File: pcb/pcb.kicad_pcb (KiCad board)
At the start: 4 copper layers, 40 x 15 mm, 20 parts, among them J1 Conn_01x04_MountingPin, J2 Conn_01x04_MountingPin, J4 Conn_ARM_SWD_TagConnect_TC203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, U1 MCP2542FDxMF, U2 STM32G0B1KBUx, U3 MCP1792x-3302xCB

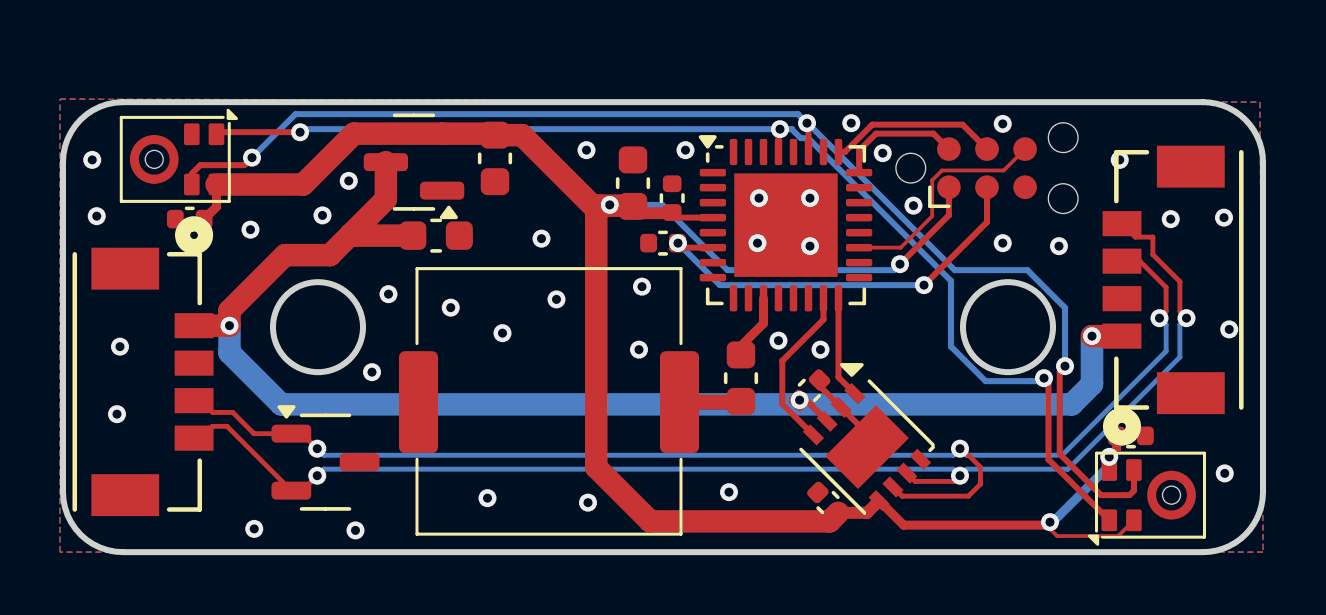
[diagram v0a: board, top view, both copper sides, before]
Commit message: add source termination
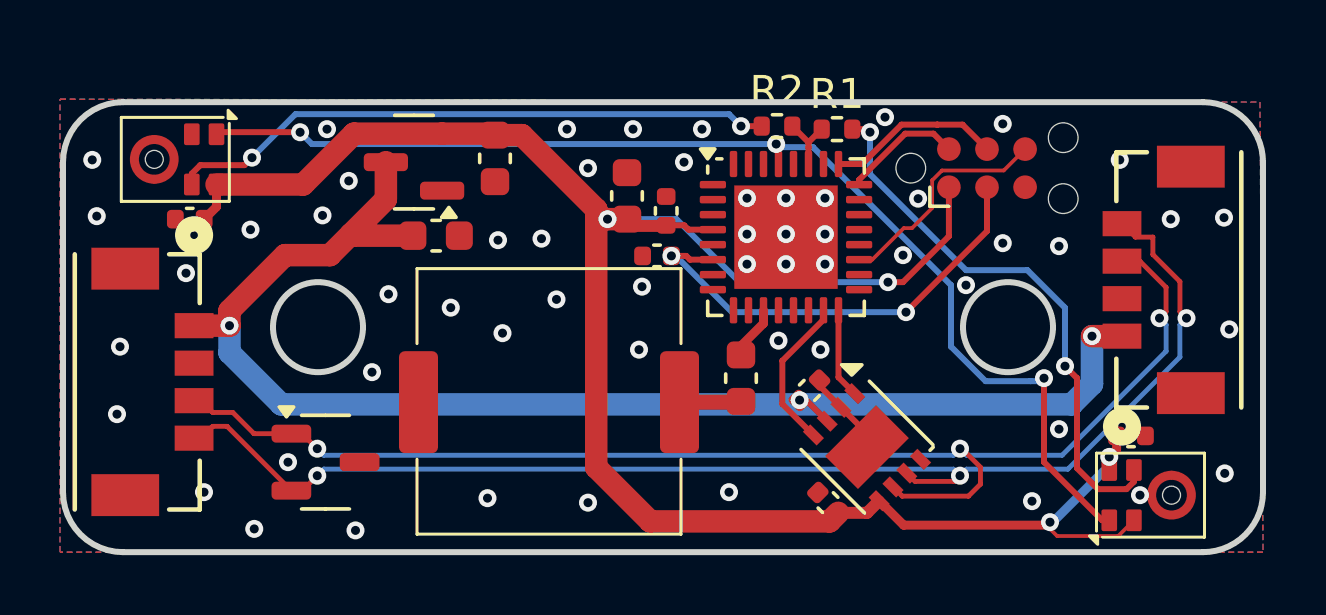
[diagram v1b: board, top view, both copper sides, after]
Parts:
- added R1: R_Small, Resistor_SMD:R_0402_1005Metric, F.Cu at (204.5, 52.5)
- added R2: R_Small, Resistor_SMD:R_0402_1005Metric, F.Cu at (202.5, 52.4)
- moved C11 0.47 mm to (198.5, 56.7)
- moved C12 0.47 mm to (198.8, 55.2)
- moved C13 0.47 mm to (197.5, 54.7)
- moved U2 0.40 mm to (202.8, 56.1)
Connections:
- M3 pad 4: /I2S_CLK -> Net-(M3-CLK)
- M4 pad 4: /I2S_CLK -> Net-(M4-CLK)
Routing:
- net /I2S_CLK: track 42.7 -> 2.11 mm, vias 3 -> 0
- net Net-(M3-CLK): track 0.00 -> 20.3 mm, vias 0 -> 2
- net Net-(M4-CLK): track 0.00 -> 18.6 mm, vias 0 -> 2
- net /RESET: track 14.2 -> 15.3 mm
- net +3V3: track 66.1 -> 67.0 mm
- net GND: vias 39 -> 56

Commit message: fix drc
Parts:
- moved C13 0.55 mm to (197.9, 54.4)
- moved C12 0.51 mm to (199.2, 54.9)
- moved C11 0.33 mm to (198.5, 56.4)
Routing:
- net GND: vias 56 -> 53

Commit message: add rs485
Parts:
- removed C10, C9: 100n, Capacitor_SMD:C_0402_1005Metric
- C1, C2: value 2.2u -> 10u
- C12, C15, C16: value 100n -> 10u
- C13: value 4.7u -> 10u
- D1: value CAN_TVS -> TVS
- LS1: moved to B.Cu
- U1: value MCP2542FDxMF -> THVD1451; footprint Package_DFN_QFN:DFN-8-1EP_3x3mm_P0.65mm_EP1.55x2.4mm -> Package_SON:VSON-10-1EP_3x3mm_P0.5mm_EP1.65x2.4mm
- U3: value MCP1792x-3302xCB -> AP2210; footprint Package_TO_SOT_SMD:SOT-23 -> Package_TO_SOT_SMD:SOT-23-3
- moved LS1 4.52 mm to (198.6, 59.0), turned to -90 degrees
- moved C14 1.35 mm to (200.0, 60.5), turned to 180 degrees
- moved U1 1.00 mm to (206.5, 63.1)
- moved R1 0.12 mm to (204.6, 52.4), turned to 180 degrees
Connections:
- net /CAN_RX renamed /TX
- net /CAN_TX renamed /RX
- net Net-(M3-CLK) renamed /CLK_1
- D1 pad 1: /CAN- -> /RS485-
- D1 pad 2: /CAN+ -> /RS485+
- J1 pad 3: /CAN- -> /RS485-
- J1 pad 4: /CAN+ -> /RS485+
- J2 pad 3: /CAN- -> /RS485-
- J2 pad 4: /CAN+ -> /RS485+
- M4 pad 4: Net-(M4-CLK) -> /CLK_2
- R1 pad 1: /I2S_CLK -> /CLK_2
- R1 pad 2: Net-(M4-CLK) -> Net-(U2-PB3)
- R2 pad 2: /I2S_CLK -> Net-(U2-PB3)
- U1 pad 2: GND -> /RX_EN
- U1 pad 3: +5V -> /TX_EN
- U1 pad 5: +3V3 -> /TERM
- U1 pad 6: /CAN- -> GND
- U1 pad 7: /CAN+ -> /SLR
- U1 pad 8: /STBY -> /RS485+
- U1 pad 9: GND -> /RS485-
- U2 pad 12: unconnected-(U2-PA5-Pad12) -> /SLR
- U2 pad 13: unconnected-(U2-PA6-Pad13) -> /TERM
- U2 pad 14: unconnected-(U2-PA7-Pad14) -> /TX_EN
- U2 pad 17: unconnected-(U2-PB2-Pad17) -> /RX_EN
- U2 pad 27: /I2S_CLK -> Net-(U2-PB3)
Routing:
- net /RS485+: track 0.00 -> 44.8 mm, vias 0 -> 3
- net /CAN+: track 43.7 -> 0.00 mm, vias 3 -> 0
- net /CAN-: track 43.6 -> 0.00 mm, vias 3 -> 0
- net /RS485-: track 0.00 -> 42.4 mm, vias 0 -> 3
- net /CLK_2: track 0.00 -> 18.8 mm, vias 0 -> 2
- net Net-(M4-CLK): track 18.6 -> 0.00 mm, vias 2 -> 0
- net +3V3: track 66.7 -> 54.5 mm
- net /SLR: track 0.00 -> 11.5 mm
- net Net-(C14-Pad2): track 2.08 -> 7.50 mm, vias 0 -> 1
- net /RX_EN: track 0.00 -> 5.40 mm, vias 0 -> 2
- net /TERM: track 0.00 -> 5.07 mm
- net /TX_EN: track 0.00 -> 4.39 mm, vias 0 -> 2
- net Net-(U2-PB3): track 0.00 -> 2.11 mm
- net /I2S_CLK: track 2.11 -> 0.00 mm
- net /RESET: track 14.8 -> 16.7 mm
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
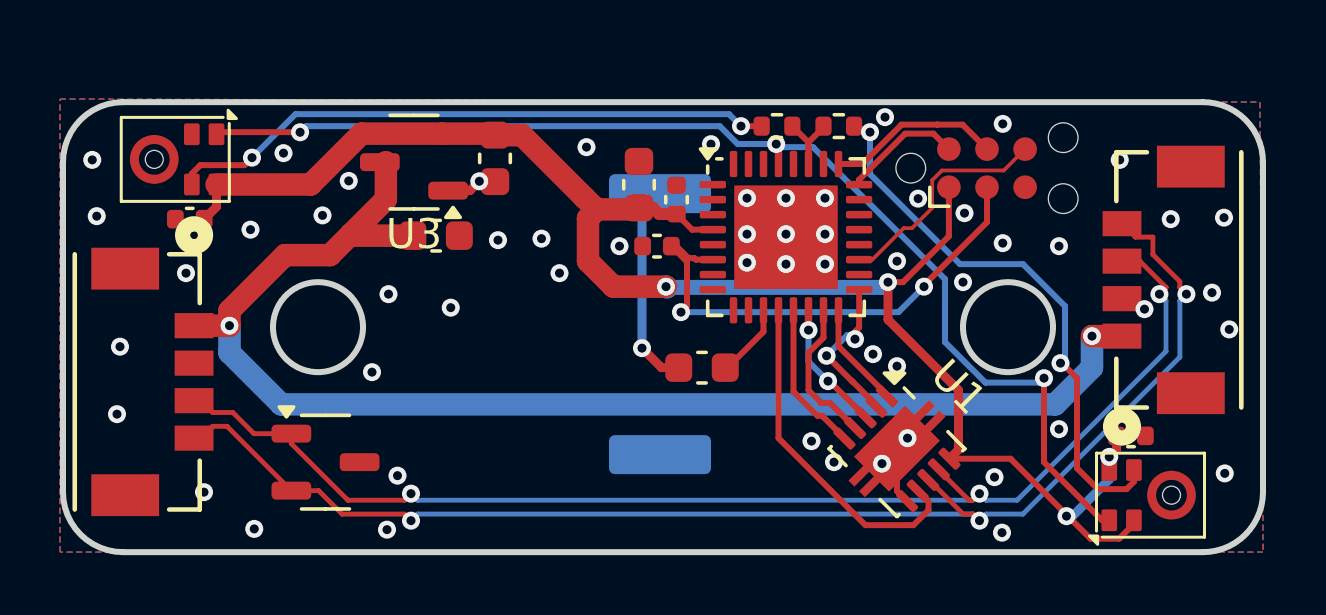
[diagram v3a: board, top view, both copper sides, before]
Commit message: rs485 re route
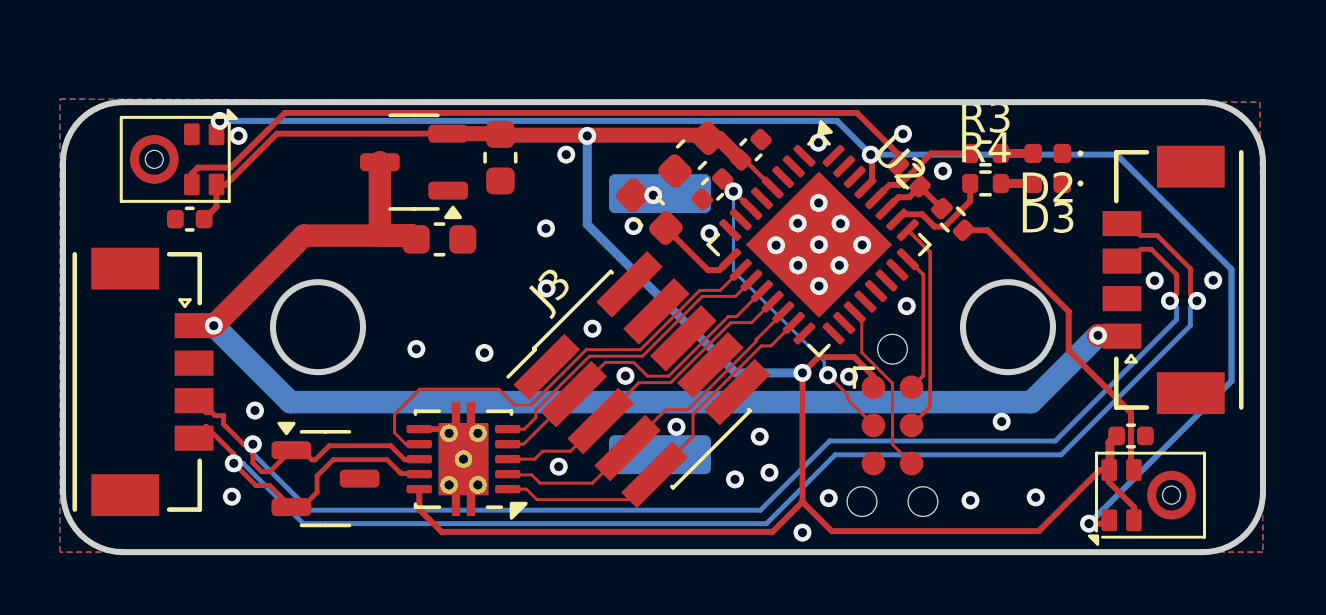
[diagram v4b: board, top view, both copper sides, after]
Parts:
- added D2: LED, Diode_SMD:D_0402_1005Metric, F.Cu at (211.5, 53.3)
- added D3: LED, Diode_SMD:D_0402_1005Metric, F.Cu at (211.5, 54.3)
- added J3: DEBUG, Connector_PinHeader_1.27mm:PinHeader_2x05_P1.27mm_Vertical_SMD, F.Cu at (198.0, 60.9)
- added R3: R_Small, Resistor_SMD:R_0402_1005Metric, F.Cu at (209.4, 53.3)
- added R4: R_Small, Resistor_SMD:R_0402_1005Metric, F.Cu at (209.4, 54.3)
- U1: footprint Package_SON:VSON-10-1EP_3x3mm_P0.5mm_EP1.65x2.4mm -> Package_SON:VSON-10-1EP_3x3mm_P0.5mm_EP1.65x2.4mm_ThermalVias
- moved U1 14.5 mm to (192.1, 63.5), turned to 180 degrees
- moved J4 9.14 mm to (206.3, 62.4), turned to -90 degrees
- moved C14 5.49 mm to (198.2, 55.2), turned to 135 degrees
- moved R1 4.91 mm to (208.4, 55.5), turned to 135 degrees
- moved R2 4.70 mm to (206.9, 54.1), turned to -45 degrees
- moved C12 2.99 mm to (201.6, 53.2), turned to 45 degrees
- moved C11 2.65 mm to (200.3, 54.5), turned to 45 degrees
- moved C13 2.02 mm to (199.7, 53.4), turned to -135 degrees
- moved U2 1.13 mm to (203.9, 56.4), turned to -45 degrees
- moved D1 0.55 mm to (187.4, 64.2)
- moved C1 0.18 mm to (193.3, 53.5)
- moved C2 0.17 mm to (191.2, 56.2)
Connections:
- D1 pad 1: /RS485- -> /RS485+
- D1 pad 2: /RS485+ -> /RS485-
- J1 pad 3: /RS485- -> /RS485+
- J1 pad 4: /RS485+ -> /RS485-
- J2 pad 3: /RS485- -> /RS485+
- J2 pad 4: /RS485+ -> /RS485-
- U2 pad 10: unconnected-(U2-PA3-Pad10) -> /SLR
- U2 pad 11: /SPEAKER -> /TERM
- U2 pad 12: /SLR -> /TX
- U2 pad 13: /TERM -> /TX_EN
- U2 pad 14: /TX_EN -> /RX_EN
- U2 pad 15: /TX -> /RX
- U2 pad 16: /RX -> unconnected-(U2-PB1-Pad16)
- U2 pad 17: /RX_EN -> unconnected-(U2-PB2-Pad17)
- U2 pad 26: unconnected-(U2-PA15-Pad26) -> /LED_2
- U2 pad 28: unconnected-(U2-PB4-Pad28) -> /LED_1
- U2 pad 9: unconnected-(U2-PA2-Pad9) -> /SPEAKER
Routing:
- net +3V3: track 54.5 -> 69.9 mm, vias 4 -> 2
- net /I2S_SD: track 39.0 -> 48.6 mm
- net /RX: track 3.53 -> 12.6 mm
- net /RS485-: track 42.4 -> 50.6 mm, vias 3 -> 2
- net /CLK_2: track 18.8 -> 10.8 mm, vias 2 -> 0
- net Net-(C14-Pad2): track 7.50 -> 0.67 mm
- net /TX_EN: track 4.39 -> 11.0 mm, vias 2 -> 0
- net /RX_EN: track 5.40 -> 11.7 mm, vias 2 -> 0
- net /TX: track 4.95 -> 11.0 mm
- net /RESET: track 16.7 -> 11.1 mm
- net /CLK_1: track 20.3 -> 25.7 mm, vias 2 -> 0
- net /TERM: track 5.07 -> 10.3 mm
- net /SLR: track 11.5 -> 15.6 mm
- net /LED_1: track 0.00 -> 3.76 mm
- net /LED_2: track 0.00 -> 3.62 mm
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
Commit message: small tweaks
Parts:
- added C3: 10u, Capacitor_SMD:C_0402_1005Metric, F.Cu at (191.2, 65.6)
- added TP1: CLK, goatworks-footprint-library:tp-ev24, F.Cu at (208.3, 53.8)
- added TP2: GND, goatworks-footprint-library:tp-ev24, F.Cu at (191.9, 57.8)
- added TP4: SD, goatworks-footprint-library:tp-ev24, F.Cu at (217.3, 57.0)
- added TP5: 5V, goatworks-footprint-library:tp-ev24, F.Cu at (189.2, 55.9)
- added TP6: 3V3, goatworks-footprint-library:tp-ev24, F.Cu at (196.2, 53.0)
- added TP7: GND, goatworks-footprint-library:tp-ev24, F.Cu at (210.2, 55.0)
- added TP8: GND, goatworks-footprint-library:tp-ev24, F.Cu at (217.3, 55.2)
- moved D2 1.00 mm to (212.1, 52.5)
- moved R3 1.00 mm to (210.0, 52.5)
- moved R4 0.89 mm to (210.0, 53.6)
- moved D3 0.89 mm to (212.1, 53.6)
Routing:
- net Net-(U2-PB3): track 2.46 -> 3.73 mm
- net /LED_2: track 3.62 -> 4.60 mm
- net /LED_1: track 3.76 -> 4.68 mm
- net +3V3: track 69.9 -> 70.6 mm, vias 2 -> 1
- net /RS485+: track 48.4 -> 48.9 mm
- net GND: vias 38 -> 63
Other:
- board text added: "--> reversible"
- board text added: "Horse With Wigs"
- board text added: "Test points requested <--- by the audio team"

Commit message: silkscreen
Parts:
- U1: footprint Package_SON:VSON-10-1EP_3x3mm_P0.5mm_EP1.65x2.4mm_ThermalVias -> Package_SON:VSON-10-1EP_3x3mm_P0.5mm_EP1.65x2.4mm
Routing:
- net Net-(C14-Pad2): track 0.67 -> 2.32 mm
- net GND: vias 63 -> 67
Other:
- board text added: "( ) (@@) ( ) (@) () @@ O @ O @ O (@@@) ( ) (@@@@) ( ) ++ +------ ____ ____________________ ____________________ || |+-+ | | \@@@@@@@@@@@ | ___ ___ ___ ___ | | ___ ___ ___ ___ | /---------|| | | | \@@@@@@@@@@@@@_ | |_| |_| |_| |_| | | |_| |_| |_| |_| | + ======== +-+ | | | |__________________| |__________________| _|--/~\------/~\-+ |__________________| |__________________| |__________________| //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"
